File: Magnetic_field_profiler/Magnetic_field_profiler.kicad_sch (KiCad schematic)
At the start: 71 parts, among them J1 USB_B_Micro, J2 Screw_Terminal_01x02, J3 Conn_01x04_Socket, J4 Conn_01x04_Socket, Q1 BSS123, SW1 SW_SPDT, U1 STM32F103C8Tx, U2 AP63203WU, U3 MCP23S17, U4 DRV8825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

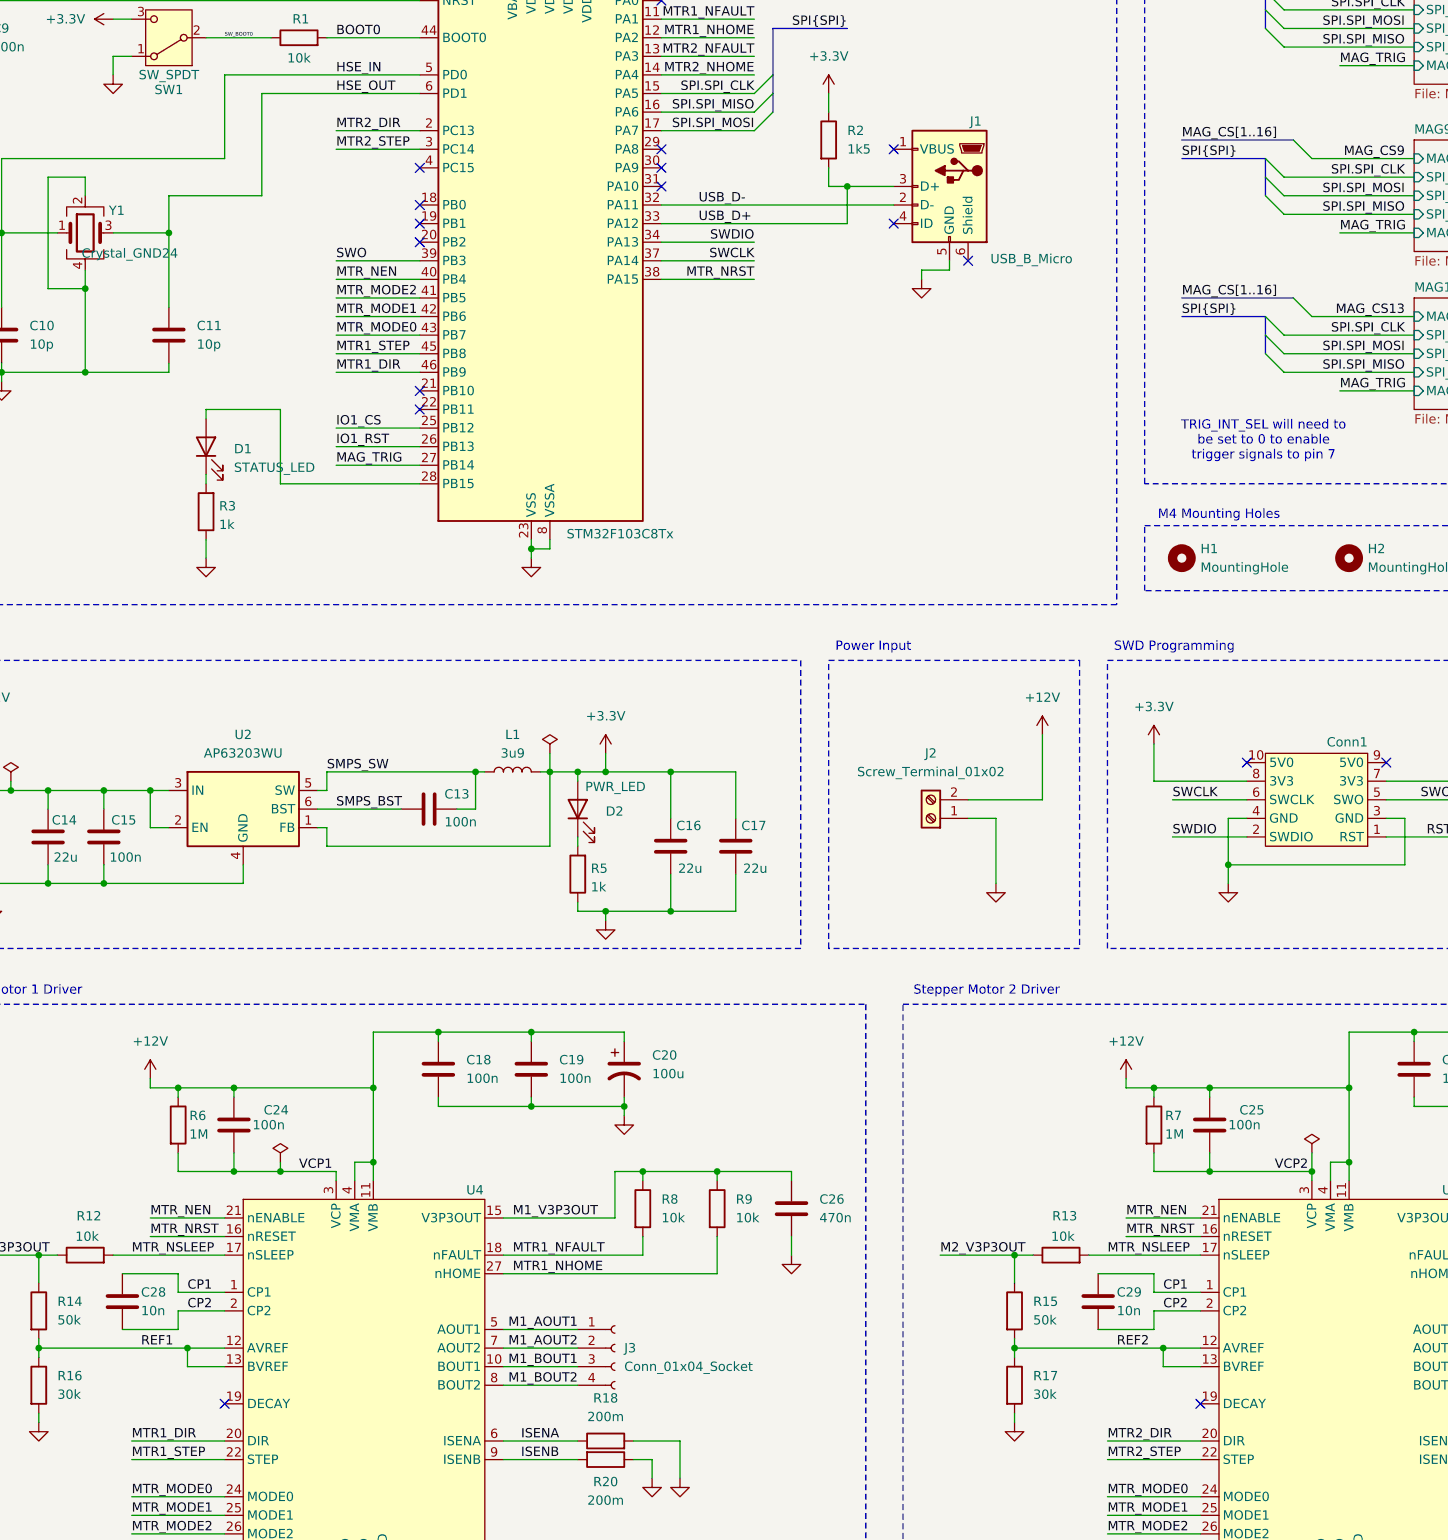
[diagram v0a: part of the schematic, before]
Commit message: Added control over motor controller decay line
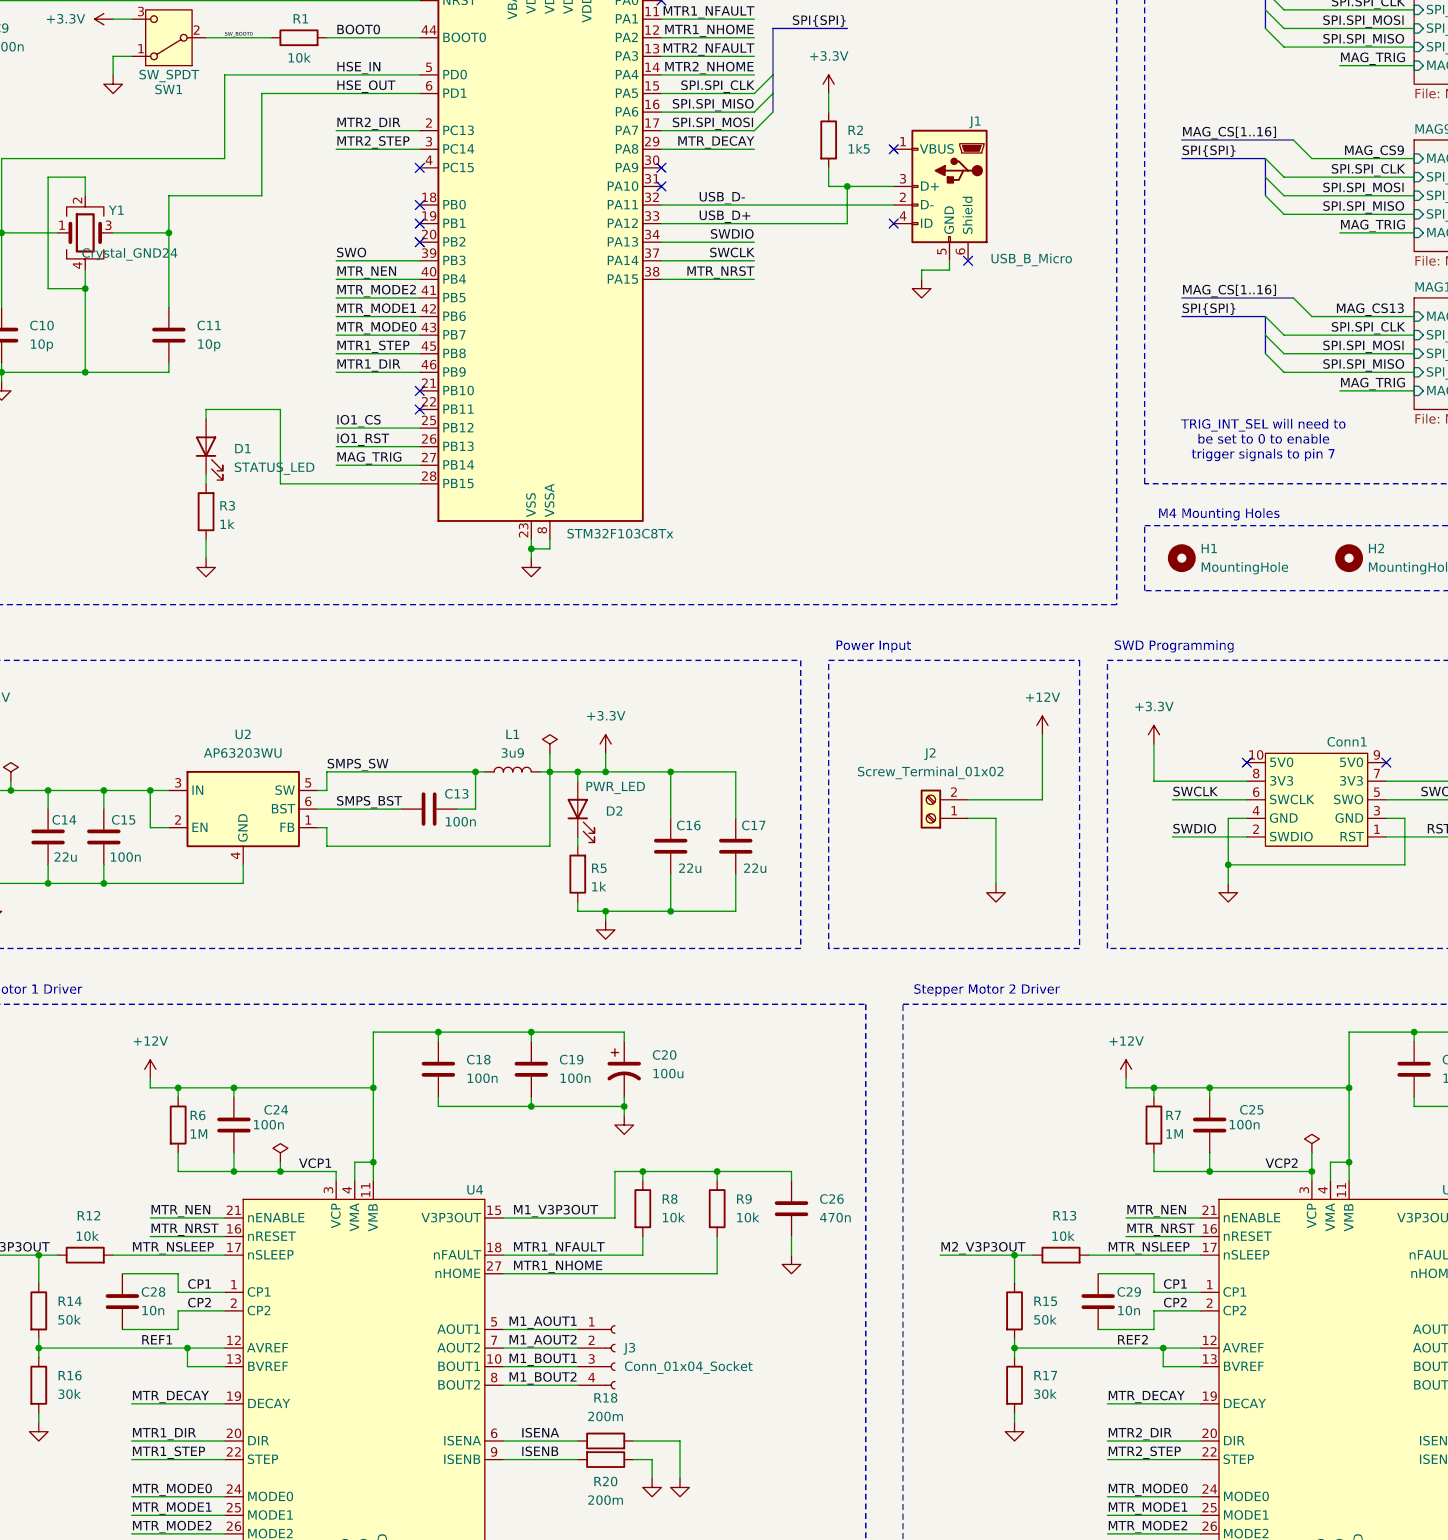
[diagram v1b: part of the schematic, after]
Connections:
- net MTR_DECAY: now reaches U4.19 (DECAY)
- net MTR_DECAY: now also U1.29 (PA8), U5.19 (DECAY)
- no-connect marks 19 -> 16
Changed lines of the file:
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@@
 	)
 	(no_connect
-		(at 58.42 241.3)
-	)
-	(no_connect
 		(at 85.09 82.55)
 	)
@@
 	)
 	(no_connect
-		(at 118.11 69.85)
-	)
-	(no_connect
 		(at 118.11 72.39)
 	)
@@
 	)
 	(no_connect
-		(at 191.77 241.3)
-	)
-	(no_connect
 		(at 85.09 102.87)
 	)
@@
 	(wire
 		(pts
+			(xy 179.07 241.3) (xy 191.77 241.3)
+		)
+		(stroke
+			(width 0)
+			(type default)
+		)
+	)
+	(wire
+		(pts
 			(xy 179.07 246.38) (xy 191.77 246.38)
 		)
@@
 	(wire
 		(pts
+			(xy 118.11 69.85) (xy 130.81 69.85)
+		)
+		(stroke
+			(width 0)
+			(type default)
+		)
+	)
+	(wire
+		(pts
 			(xy 251.46 55.88) (xy 269.24 55.88)
 		)
@@
 	(wire
 		(pts
+			(xy 45.72 241.3) (xy 58.42 241.3)
+		)
+		(stroke
+			(width 0)
+			(type default)
+		)
+	)
+	(wire
+		(pts
 			(xy 203.2 100.33) (xy 220.98 100.33)
 		)
@@
 		)
 	)
+	(label "MTR_DECAY"
+		(at 45.72 241.3 0)
+		(fields_autoplaced yes)
+		(effects
+			(font
+				(size 1.27 1.27)
+			)
+			(justify left bottom)
+		)
+	)
 	(label "MAG_CS16"
 		(at 369.57 92.71 180)
@@
 		)
 	)
+	(label "MTR_DECAY"
+		(at 130.81 69.85 180)
+		(fields_autoplaced yes)
+		(effects
+			(font
+				(size 1.27 1.27)
+			)
+			(justify right bottom)
+		)
+	)
 	(label "MAG_TRIG"
 		(at 259.08 81.28 0)
@@
 	)
 	(label "VCP2"
-		(at 201.93 209.55 0)
+		(at 200.66 209.55 0)
 		(fields_autoplaced yes)
 		(effects
@@
 		)
 	)
+	(label "MTR_DECAY"
+		(at 179.07 241.3 0)
+		(fields_autoplaced yes)
+		(effects
+			(font
+				(size 1.27 1.27)
+			)
+			(justify left bottom)
+		)
+	)
